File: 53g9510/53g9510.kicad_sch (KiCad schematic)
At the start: 115 parts, among them IC2 TC54VC3902MB, IC3 "EEF", IC4 "AQ", IC5 LM358, IC6 LM393, J1 TO FLEX, J10 CELL_NEG1, J11 CELL_NEG2, J12 BAT_CS, J13 nc, J14 BAT_CS, J15 THERM2A, J16 THERM2B, J17 BAT_POS, J18 BAT_TAP, J19 CELL_NEG1, J2 TO J1, J20 CELL_NEG2, J3 BAT_TAP, J4 BAT_POS, J5 THERM1A, J6 THERM1B, J7 BAT_POS, J8 THERM, J9 BAT_NEG, Q1 2SJ238, Q2 2SK1717, Q3 "XE", Q4 "XE", Q5 "VF", SW1 SW_SPST, U1 TMP47C241, X1 2MHz

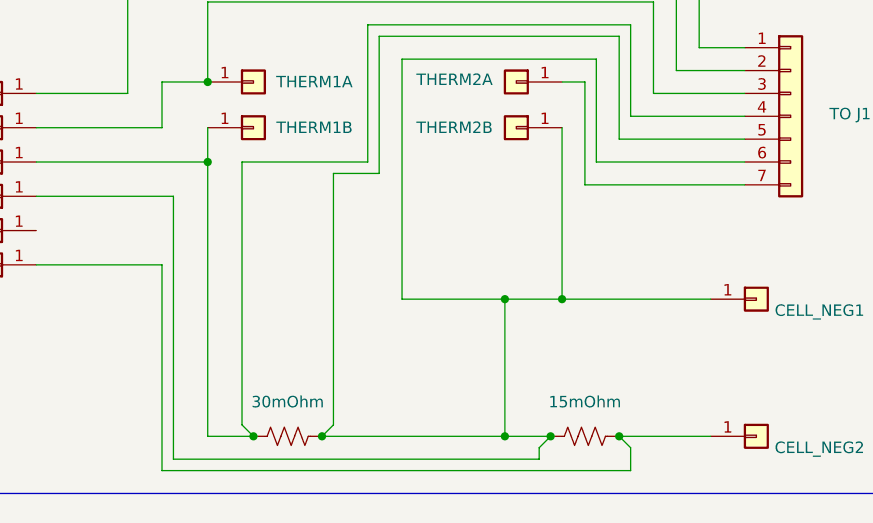
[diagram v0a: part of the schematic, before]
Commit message: Add flex circuit to 53g9510
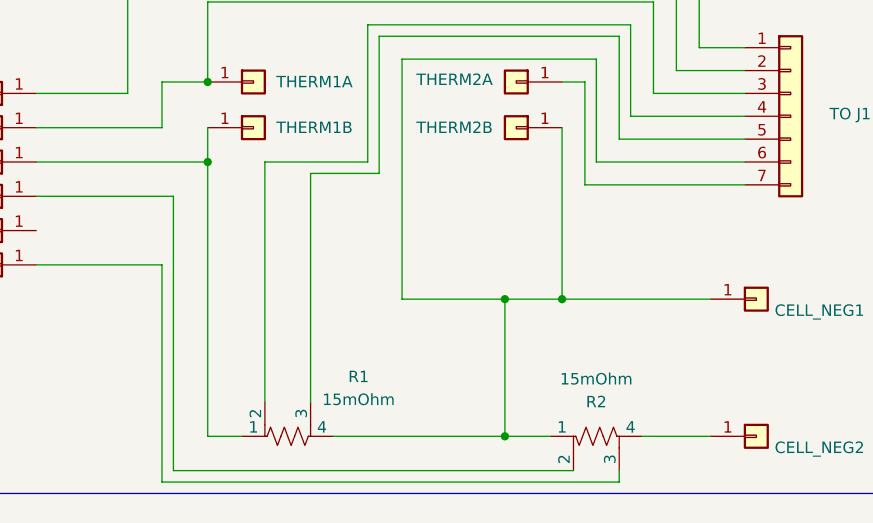
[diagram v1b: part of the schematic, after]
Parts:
- removed R1: 30mOhm, symbol Device:R_US
- removed R2: 15mOhm, symbol Device:R_US
- added R1: 15mOhm, 700CPowerBoard:RES_CS_2, symbol Device:R_Shunt_US
- added R2: 15mOhm, 700CPowerBoard:RES_CS_1, symbol Device:R_Shunt_US
- J1, J2: footprint Connector_JST:JST_ZE_BM07B-ZESS-TBT_1x07-1MP_P1.50mm_Vertical -> 700CPowerBoard:FLEXCONN_1_5MM
- J10, J11, J12, J13, J14, J15, J16, J4, J6, J7, J8, J9: footprint (none) -> 700CPowerBoard:PAD_5_5mm
- J3: footprint (none) -> 700CPowerBoard:PAD_5_4mm
- J5: footprint (none) -> 700CPowerBoard:PAD_5_3mm
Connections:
- net at J10.1 (Pin_1), J16.1 (Pin_1), J2.6 (Pin_6): now also R1.4, R2.1; no longer J12.1 (Pin_1), J2.5 (Pin_5)
- net at J14.1 (Pin_1): now also R2.3; no longer J11.1 (Pin_1)
- net at J6.1 (Pin_1), J9.1 (Pin_1): now also R1.1; no longer J2.4 (Pin_4)
- new net: J12.1 (Pin_1), R2.2
- new net: J11.1 (Pin_1), R2.4
- new net: J2.4 (Pin_4), R1.2
- new net: J2.5 (Pin_5), R1.3
